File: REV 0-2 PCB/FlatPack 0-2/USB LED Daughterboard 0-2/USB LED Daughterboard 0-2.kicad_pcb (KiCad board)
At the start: 2 copper layers, 60 parts, among them J1 USB_C_Receptacle_USB2.0, J2 Conn_02x05_Odd_Even, Q1 SQJ479EP, U1 STUSB4500, U2 PCA9685PW

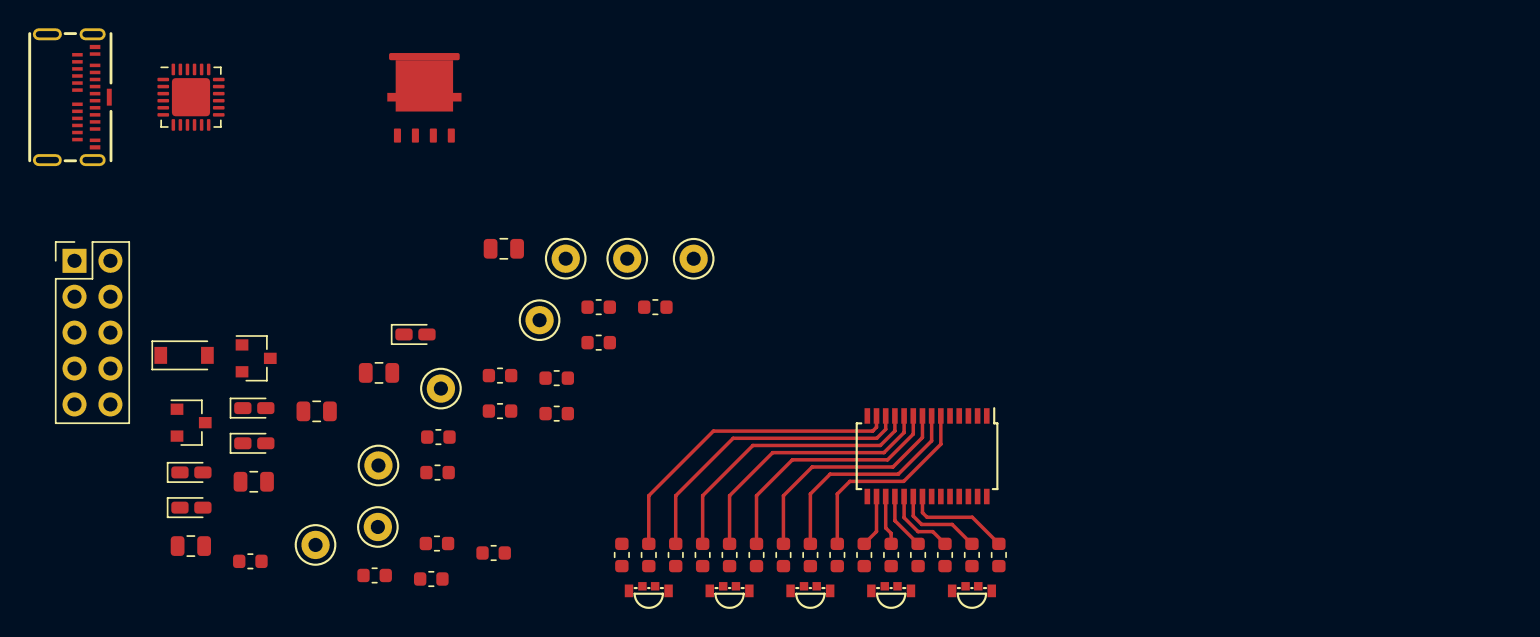
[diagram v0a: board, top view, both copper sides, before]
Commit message: More work on USB LED SubBoard
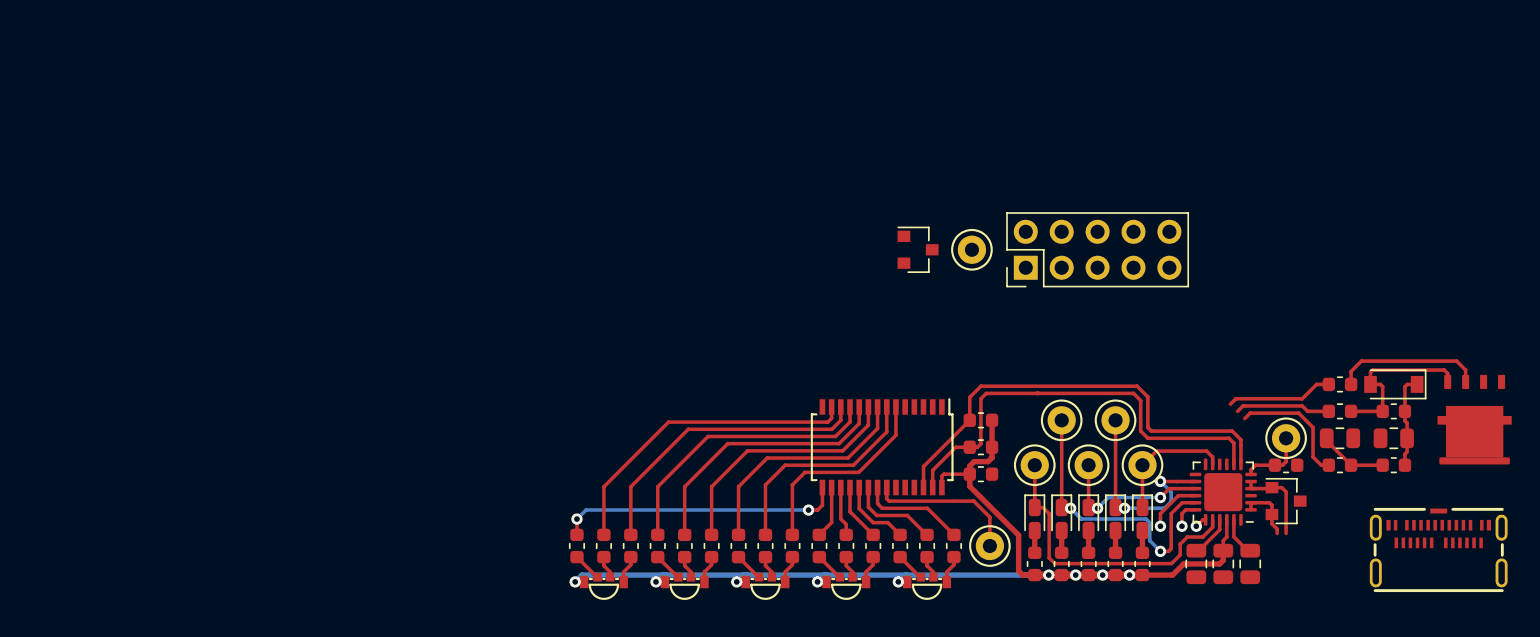
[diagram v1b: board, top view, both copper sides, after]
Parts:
- moved J1 104.0 mm to (217.8, 123.8), turned to 0 degrees
- moved D8 85.6 mm to (214.6, 110.5), turned to 180 degrees
- moved C4 81.6 mm to (210.8, 114.3), turned to 180 degrees
- moved R3 81.6 mm to (214.6, 112.4), turned to 180 degrees
- moved U1 78.2 mm to (202.6, 118.1), turned to 180 degrees
- moved Q1 77.7 mm to (220.3, 113.0), turned to 180 degrees
- moved D2 73.6 mm to (207.0, 118.7)
- moved C2 71.9 mm to (214.6, 114.3)
- moved R1 67.7 mm to (214.6, 116.2)
- moved J2 67.3 mm to (188.6, 102.2), turned to 90 degrees
- moved C3 66.9 mm to (200.7, 123.2), turned to 90 degrees
- moved C1 66.9 mm to (204.5, 123.2), turned to 90 degrees
- moved D3 65.5 mm to (194.9, 120.0), turned to 270 degrees
- moved R2 63.8 mm to (210.8, 116.2)
- moved D7 63.5 mm to (193.0, 120.0), turned to 270 degrees
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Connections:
- net Net-(D2-Pad1) renamed /CC2
- net Net-(D2-Pad2) renamed /CC1
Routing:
- net +3V3: track 0.00 -> 80.3 mm, vias 0 -> 9
- net /SCL: track 0.00 -> 31.8 mm
- net /SDA: track 0.00 -> 31.0 mm
- net /PDO2: track 0.00 -> 21.1 mm
- net /A_B: track 0.00 -> 20.5 mm, vias 0 -> 2
- net Net-(R22-Pad2): track 0.00 -> 20.1 mm, vias 0 -> 2
- net /PDO3: track 0.00 -> 14.6 mm, vias 0 -> 2
- net Net-(D8-Pad2): track 0.00 -> 12.0 mm
- net /GPIO: track 0.00 -> 11.2 mm, vias 0 -> 2
- net Net-(R2-Pad1): track 0.00 -> 10.8 mm, vias 0 -> 1
- net /CH_15: track 0.00 -> 10.7 mm
- net Net-(R9-Pad1): track 0.00 -> 10.7 mm, vias 0 -> 1
- net Net-(J2-Pad10): track 0.00 -> 10.4 mm
- net /ATTACH: track 0.00 -> 9.07 mm
- net Net-(R11-Pad2): track 0.00 -> 7.54 mm
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
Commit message: More USB LED SubBoard updates
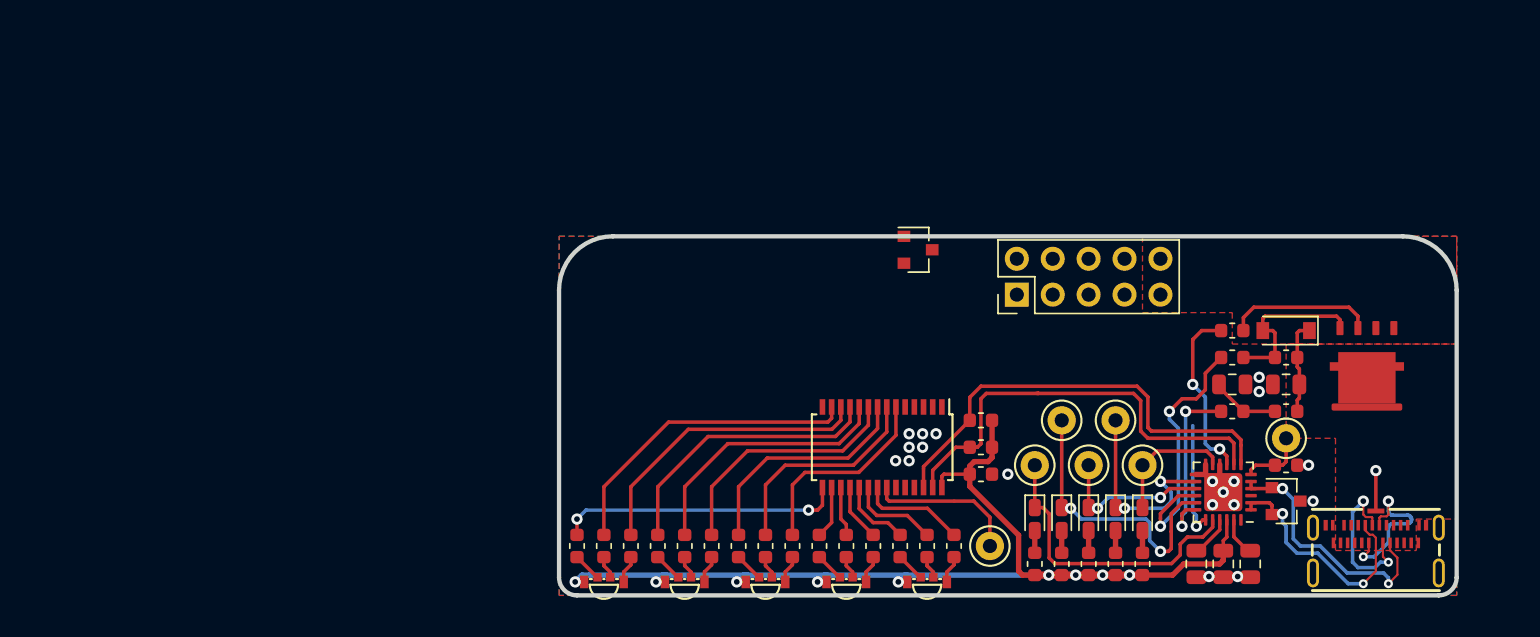
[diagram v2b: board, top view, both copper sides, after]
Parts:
- removed the TP6 at (184.8, 101.0)
- moved C2 8.52 mm to (207.0, 110.5)
- moved C4 8.52 mm to (203.2, 110.5)
- moved Q1 8.52 mm to (212.7, 109.2)
- moved R1 8.52 mm to (207.0, 112.4)
- moved R2 8.52 mm to (203.2, 112.4)
- moved R3 8.52 mm to (207.0, 108.6)
- moved R9 8.52 mm to (203.2, 108.6)
- moved D8 8.52 mm to (207.0, 106.7)
- moved R11 8.52 mm to (203.2, 106.7)
- moved J1 4.44 mm to (213.4, 123.8)
- moved J2 2.01 mm to (188.0, 104.1)
- renumbered TP7 to TP6, TP8 to TP7
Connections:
- net Net-(C2-Pad2) renamed /VBUS_IN
- net Net-(J2-Pad10) renamed /VBUS_OUT
- J1 pad A8: (no net) -> Net-(J1-PadA8)
- J1 pad B8: (no net) -> Net-(J1-PadB8)
- U1 pad 3: (no net) -> Net-(U1-Pad3)
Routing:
- net /CC1: track 4.20 -> 17.2 mm, vias 0 -> 2
- net /CC2: track 6.07 -> 18.3 mm, vias 0 -> 2
- net /D+: track 0.00 -> 11.2 mm, vias 0 -> 2
- net /D-: track 0.00 -> 11.2 mm, vias 0 -> 2
- net Net-(R9-Pad1): track 10.7 -> 18.7 mm, vias 1 -> 2
- net /ALERT: track 0.84 -> 8.06 mm
- net GND: track 0.00 -> 7.04 mm, vias 0 -> 20
- net Net-(R11-Pad2): track 7.54 -> 12.5 mm, vias 0 -> 2
- net Net-(R2-Pad1): track 10.8 -> 12.7 mm, vias 1 -> 2
- added copper zone on F.Cu, net /VBUS_IN
- added copper zone on F.Cu, net /VBUS_OUT
- added copper zone on B.Cu, net GND
- added copper zone on F.Cu, net GND
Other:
- board outline added: 63.5 x 25.4 mm
- net class Default: clearance 0.2 -> 0.127; trace_width 0.25 -> 0.127
- rule trace_clearance: 0.2 -> 0.127
- rule trace_min: 0.1524 -> 0.127

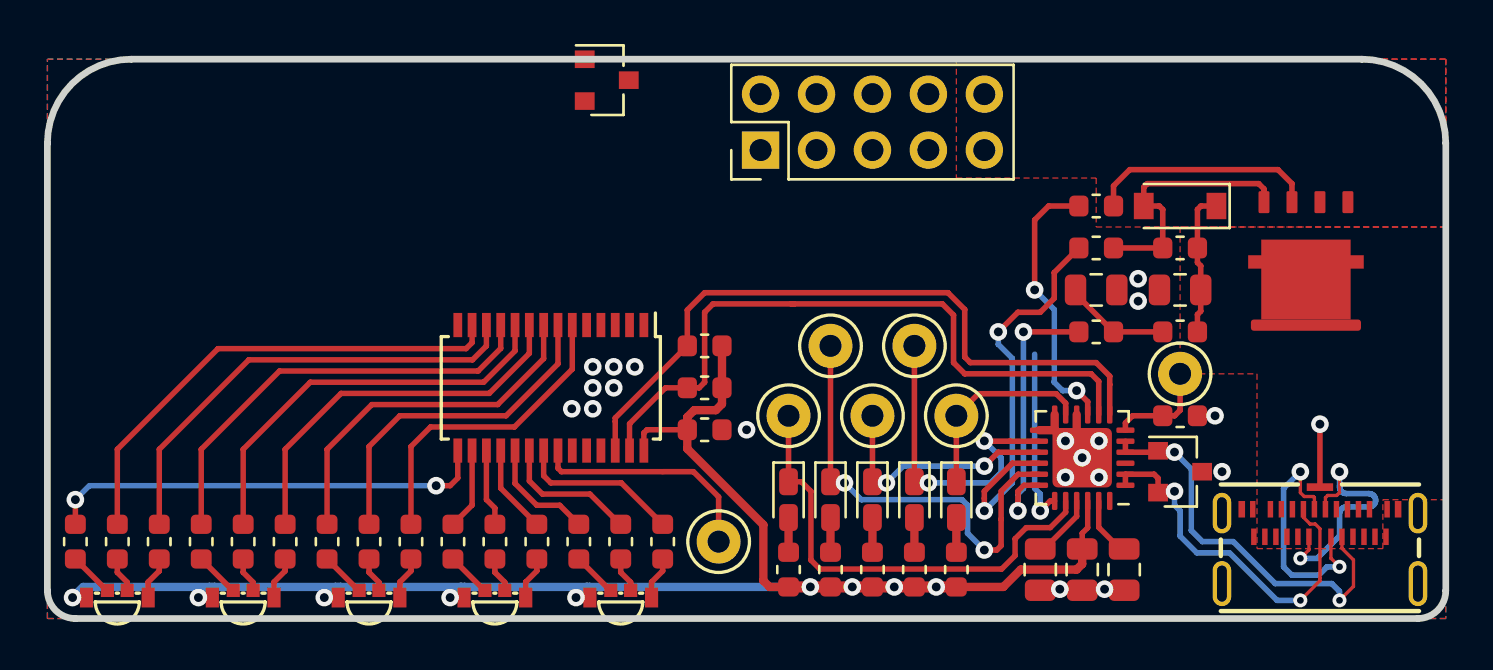
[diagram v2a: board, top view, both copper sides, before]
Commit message: Finishing USB LED Daughterboard
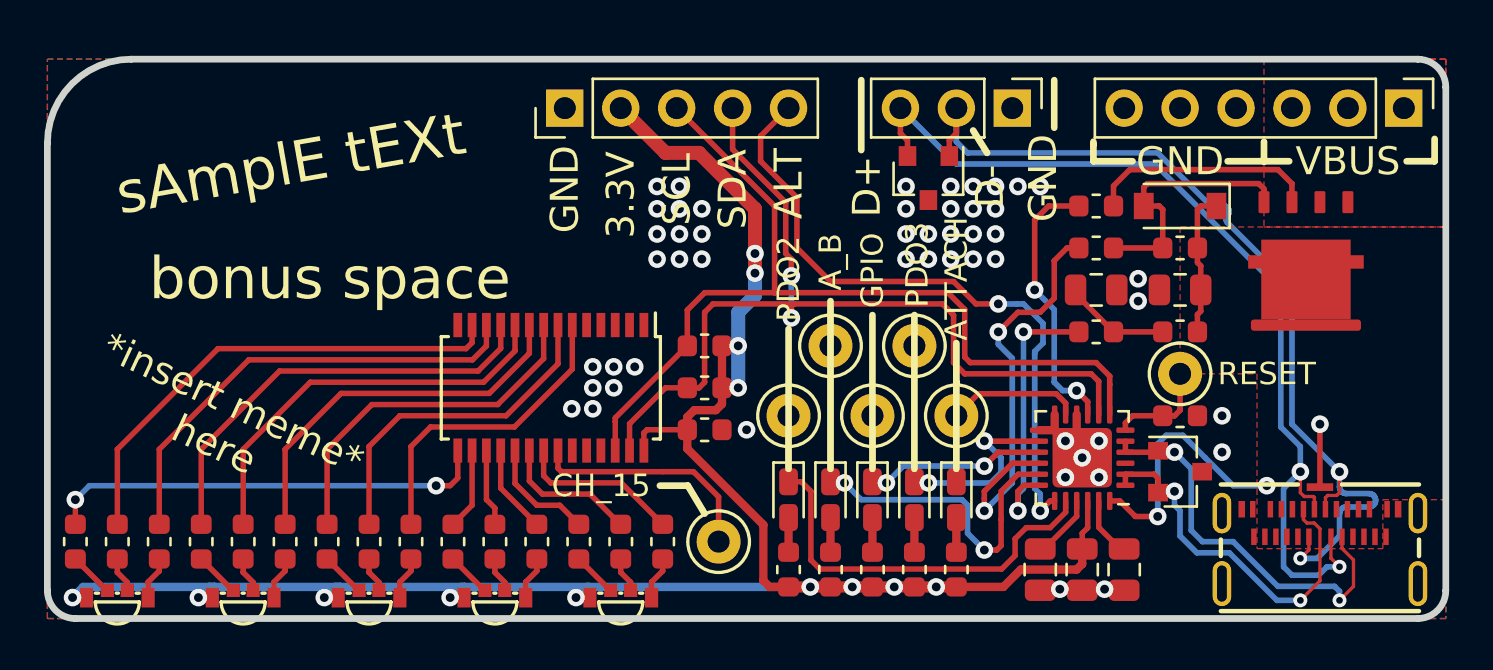
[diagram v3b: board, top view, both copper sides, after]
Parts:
- added J3: Conn_01x06, Connector_PinHeader_2.54mm:PinHeader_1x06_P2.54mm_Vertical, F.Cu at (217.2, 102.2)
- added J4: Conn_01x05, Connector_PinHeader_2.54mm:PinHeader_1x05_P2.54mm_Vertical, F.Cu at (179.1, 102.2)
- J2: value Conn_02x05_Odd_Even -> Conn_01x03; footprint Connector_PinHeader_2.54mm:PinHeader_2x05_P2.54mm_Vertical -> Connector_PinHeader_2.54mm:PinHeader_1x03_P2.54mm_Vertical
- moved D1 15.3 mm to (195.6, 105.4), turned to 270 degrees
- moved J2 11.6 mm to (199.4, 102.2), turned to 270 degrees
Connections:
- D1 pad 1: /D+ -> /D-
- D1 pad 2: /D- -> /D+
- J1 pad A8: Net-(J1-PadA8) -> (no net)
- J1 pad B8: Net-(J1-PadB8) -> (no net)
- J2 pad 1: +3V3 -> GND
- J2 pad 2: /ALERT -> /D-
- J2 pad 3: /D- -> /D+
- U1 pad 3: Net-(U1-Pad3) -> (no net)
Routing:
- net /D-: track 11.2 -> 42.9 mm
- net /D+: track 11.2 -> 42.9 mm
- net /ALERT: track 8.06 -> 29.8 mm, vias 1 -> 2
- net +3V3: track 80.3 -> 99.1 mm, vias 9 -> 13
- net /VBUS_IN: track 6.61 -> 18.4 mm, vias 0 -> 2
- net /SDA: track 31.0 -> 42.3 mm, vias 0 -> 2
- net /SCL: track 31.8 -> 42.0 mm
- net GND: vias 20 -> 51
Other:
- outline, holes or cut-outs redrawn
- board text added: "*insert meme* here"
- board text added: "3.3V"
- board text added: "ALT"
- board text added: "ATTACH"
- board text added: "A_B"
- board text added: "CH_15"
- board text added: "D+"
- board text added: "D-"
- board text added: "GND"
- board text added: "GPIO"
- board text added: "Ishaan Gov Oct 2019"
- board text added: "PDO2"
- board text added: "PDO3"
- board text added: "RESET"
- board text added: "SCL"
- board text added: "SDA"
- board text added: "USB LED SubBoard 0-3"
- board text added: "VBUS"
- board text added: "bonus space"
- board text added: "sAmplE tEXt"
